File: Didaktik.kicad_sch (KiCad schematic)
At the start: 102 parts, among them J2 Conn_01x04_MountingPin, SW1 SW_Push, SW10 SW_Push_45deg, SW11 SW_Push_45deg, SW12 SW_Push_45deg, SW13 SW_Push_45deg, SW14 SW_Push_45deg, SW15 SW_Push_45deg, SW16 SW_Push_45deg, SW17 SW_Push_45deg, SW18 SW_Push_45deg, SW19 SW_Push_45deg, SW2 SW_Push_45deg, SW20 SW_Push_45deg, SW21 SW_Push_45deg, SW22 SW_Push_45deg, SW23 SW_Push_45deg, SW24 SW_Push_45deg, SW25 SW_Push_45deg, SW26 SW_Push_45deg, SW27 SW_Push_45deg, SW28 SW_Push_45deg, SW29 SW_Push_45deg, SW3 SW_Push_45deg, SW30 SW_Push_45deg, SW31 SW_Push_45deg, SW32 SW_Push_45deg, SW33 SW_Push_45deg, SW34 SW_Push_45deg, SW35 SW_Push_45deg, SW36 SW_Push_45deg, SW37 SW_Push_45deg, SW38 SW_Push_45deg, SW39 SW_Push_45deg, SW4 SW_Push_45deg, SW40 SW_Push_45deg, SW41 SW_Push_45deg, SW5 SW_Push_45deg, SW6 SW_Push_45deg, SW7 SW_Push_45deg, SW8 SW_Push_45deg, SW9 SW_Push_45deg, U1 ATmega32U4-M, Y1 Crystal_GND24_Small

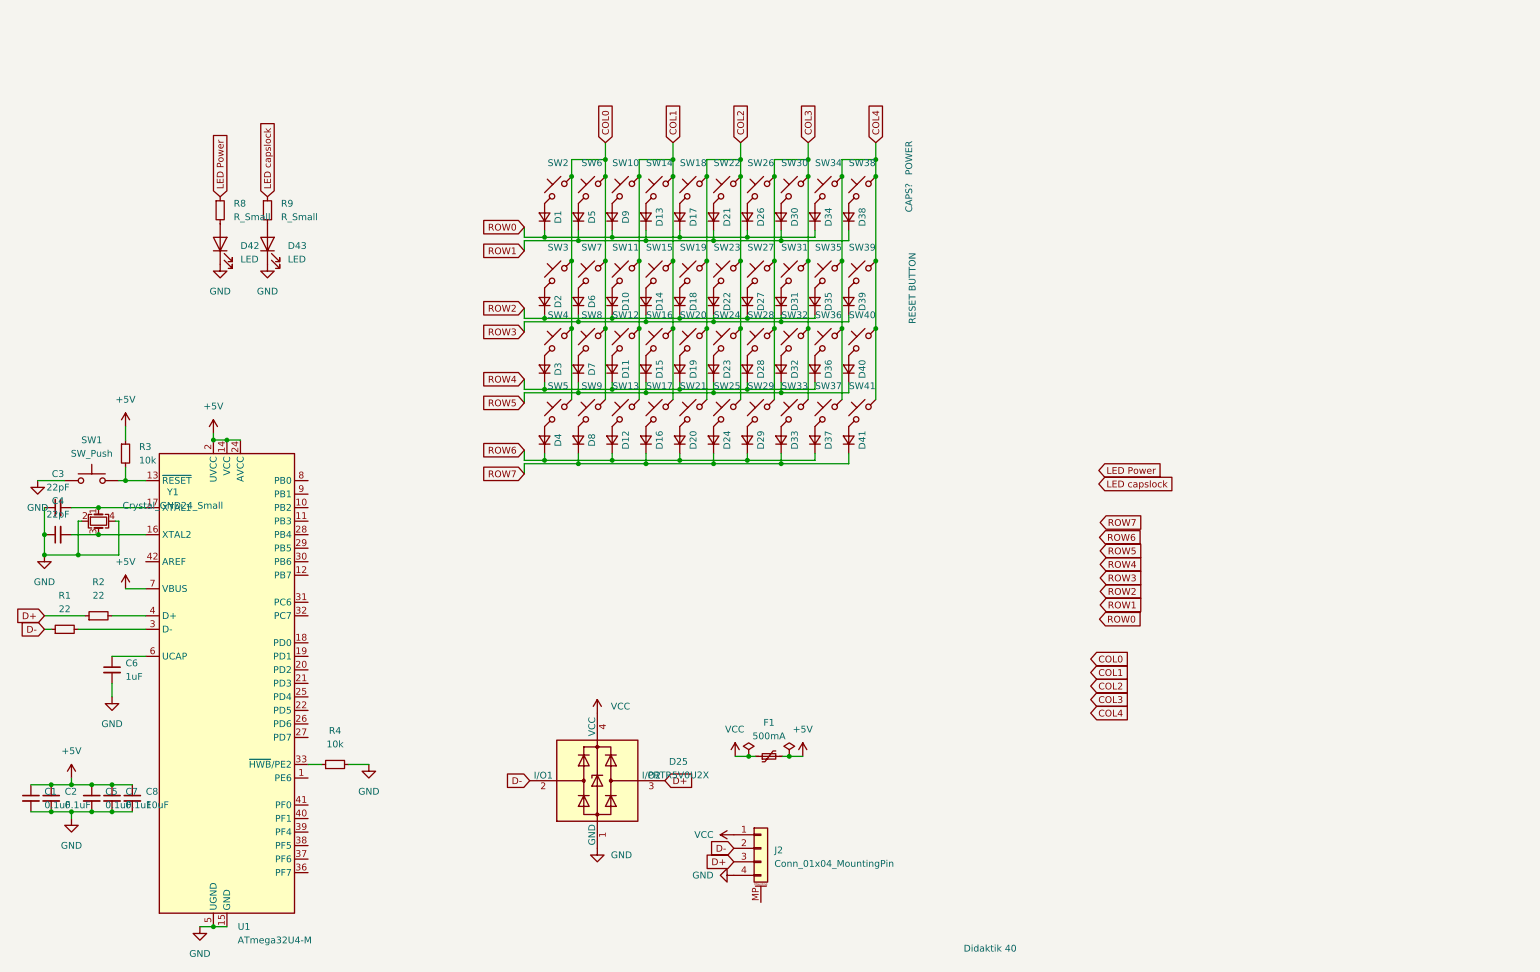
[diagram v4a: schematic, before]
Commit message: all traces routed, schematics cleaned up
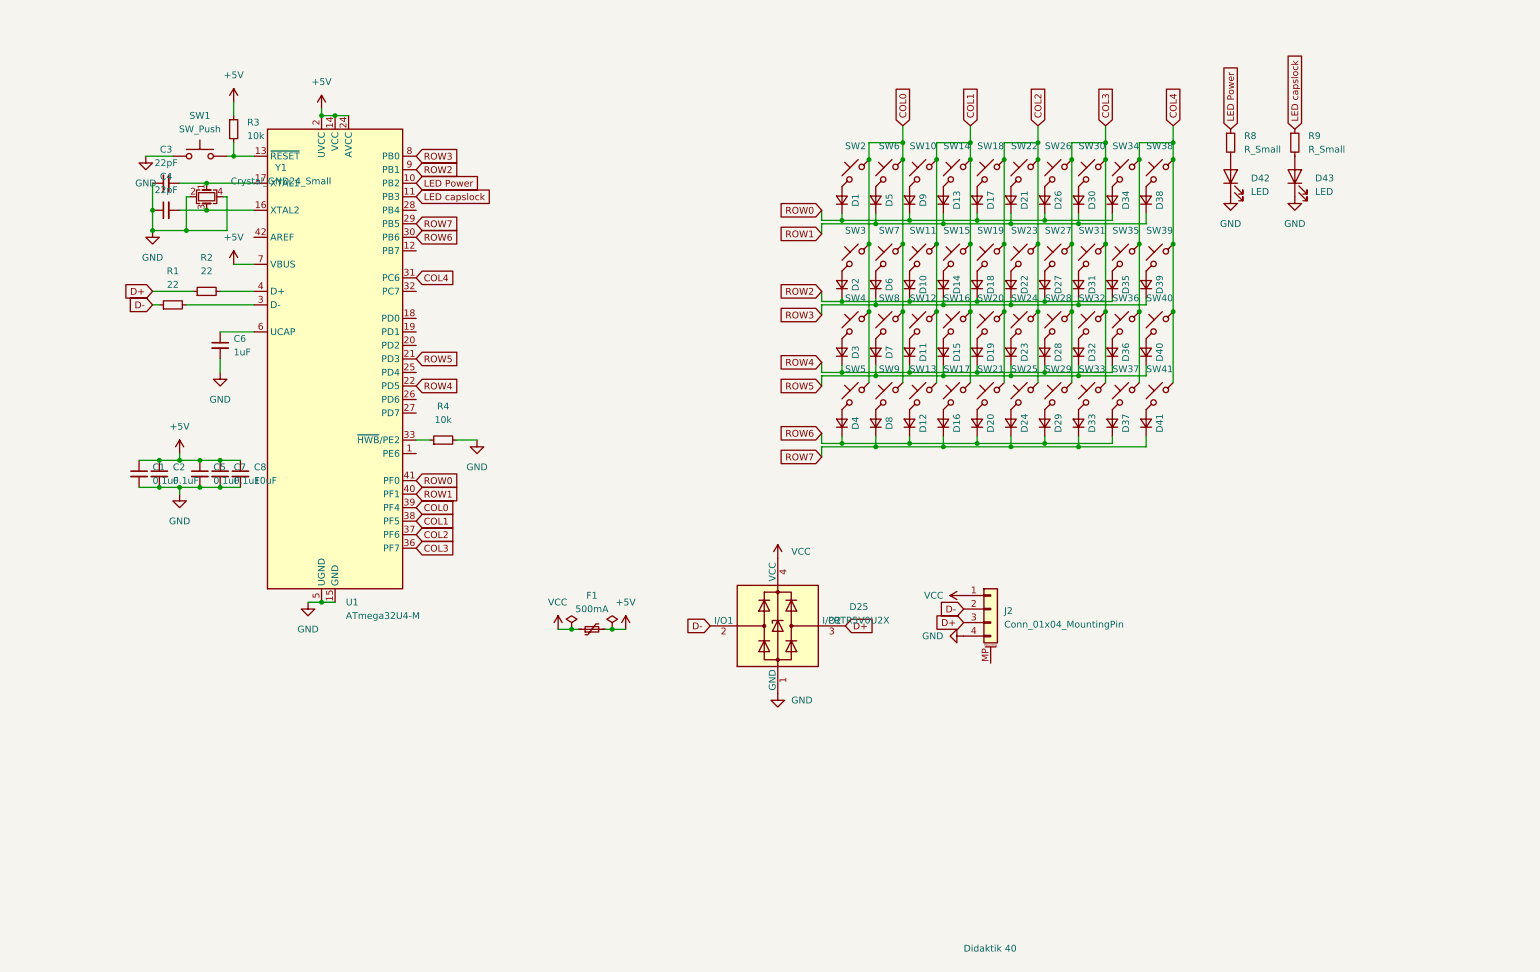
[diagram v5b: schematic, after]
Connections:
- net COL0: now also U1.39 (PF4)
- net COL1: now also U1.38 (PF5)
- net COL2: now also U1.37 (PF6)
- net COL3: now also U1.36 (PF7)
- net COL4: now also U1.31 (PC6)
- net LED Power: now also U1.10 (PB2)
- net LED capslock: now also U1.11 (PB3)
- net ROW0: now also U1.41 (PF0)
- net ROW1: now also U1.40 (PF1)
- net ROW2: now also U1.9 (PB1)
- net ROW3: now also U1.8 (PB0)
- net ROW4: now also U1.22 (PD5)
- net ROW5: now also U1.21 (PD3)
- net ROW6: now also U1.30 (PB6)
- net ROW7: now also U1.29 (PB5)
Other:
- note removed: "CAPS?"
- note removed: "POWER"
- note removed: "RESET BUTTON"
- moved on the sheet: C1, C2, C3, C4, C5, C6, C7, C8, D1, D10, D11, D12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

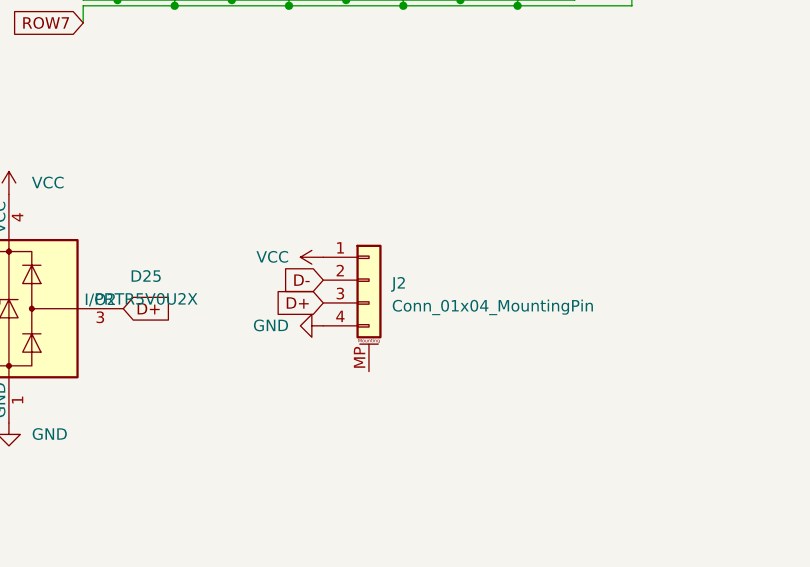
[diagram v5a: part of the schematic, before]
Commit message: full routing, silkscreens, zones
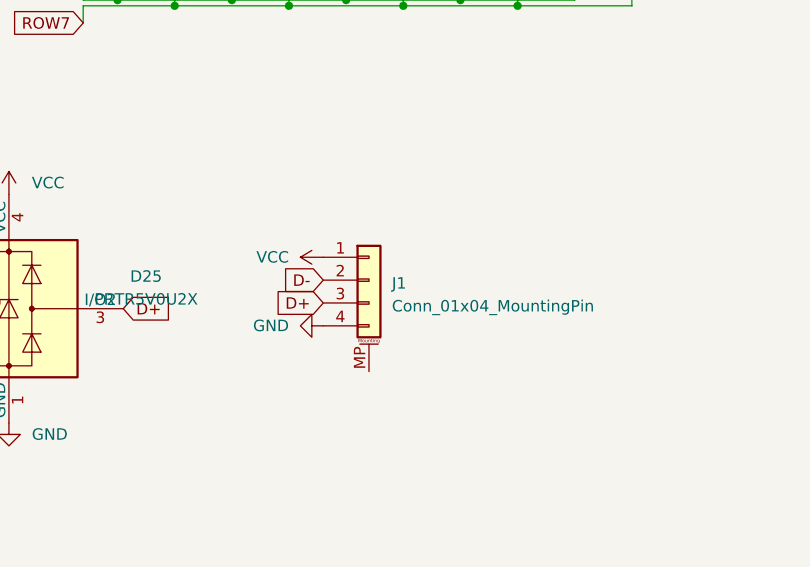
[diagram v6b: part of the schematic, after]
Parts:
- renumbered J2 to J1
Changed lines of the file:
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@@
   (symbol (lib_id "Connector_Generic_MountingPin:Conn_01x04_MountingPin") (at 193.04 125.73 0) (unit 1)
     (in_bom yes) (on_board yes) (fields_autoplaced)
-    (property "Reference" "J2" (id 0) (at 195.58 126.0855 0)
+    (property "Reference" "J1" (id 0) (at 195.58 126.0855 0)
       (effects (font (size 1.27 1.27)) (justify left))
     )
@@
     )
     (path "/773ca0f3-ad89-40fc-bb52-d706b4c154be"
-      (reference "J2") (unit 1) (value "Conn_01x04_MountingPin") (footprint "random-keyboard-parts:JST-SR-4")
+      (reference "J1") (unit 1) (value "Conn_01x04_MountingPin") (footprint "random-keyboard-parts:JST-SR-4")
     )
     (path "/1b233532-9656-4e4e-a0b7-8260db2f2d5f"

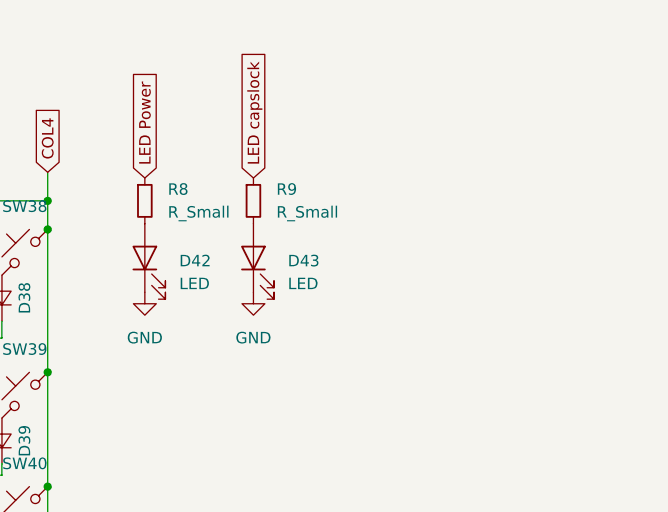
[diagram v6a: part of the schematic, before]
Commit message: created switchplate 40, cleaned 40s pcb. finished schematics for 45. created pcb project for 45
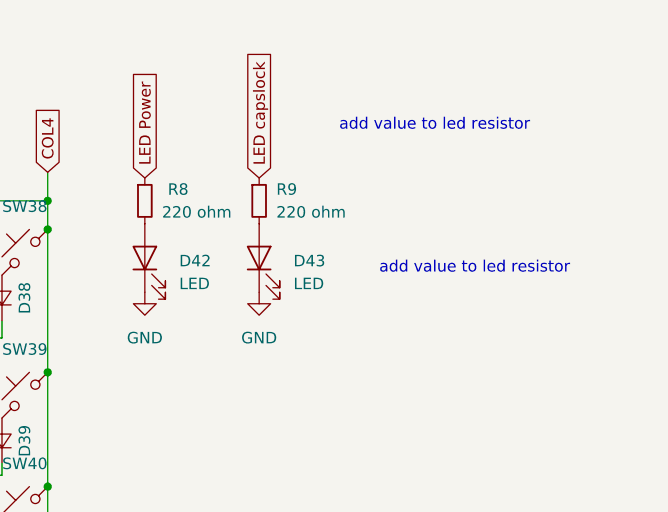
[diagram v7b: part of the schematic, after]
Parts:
- R8, R9: value R_Small -> 220 ohm
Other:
- note added: "add value to led resistor"
- moved on the sheet: D43, R9
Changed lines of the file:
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@@
+    (effects (font (size 1.27 1.27)) (justify left bottom))
+  )
+  (text "add value to led resistor" (at 259.715 30.48 0)
+    (effects (font (size 1.27 1.27)) (justify left bottom))
+  )
+  (text "add value to led resistor" (at 264.16 46.355 0)
     (effects (font (size 1.27 1.27)) (justify left bottom))
   )
@@
     )
   )
-  (global_label "LED capslock" (shape input) (at 250.19 35.56 90) (fields_autoplaced)
+  (global_label "LED capslock" (shape input) (at 250.825 35.56 90) (fields_autoplaced)
     (effects (font (size 1.27 1.27)) (justify left))
-    (property "Intersheet References" "${INTERSHEET_REFS}" (id 0) (at 250.1106 20.3864 90)
+    (property "Intersheet References" "${INTERSHEET_REFS}" (id 0) (at 250.7456 20.3864 90)
       (effects (font (size 1.27 1.27)) (justify left) hide)
     )
@@
     (pin "1")
   )
-  (symbol (lib_id "ComboDiode:R_Small") (at 250.19 38.1 0) (unit 1)
+  (symbol (lib_id "ComboDiode:R_Small") (at 250.825 38.1 0) (unit 1)
     (in_bom yes) (on_board yes) (fields_autoplaced)
     (property "Reference" "R9" (id 0) (at 252.73 36.8299 0)
       (effects (font (size 1.27 1.27)) (justify left))
     )
-    (property "Value" "R_Small" (id 1) (at 252.73 39.3699 0)
-      (effects (font (size 1.27 1.27)) (justify left))
-    )
-    (property "Footprint" "Resistor_SMD:R_0402_1005Metric" (id 2) (at 250.19 38.1 0)
-      (effects (font (size 1.27 1.27)) hide)
-    )
-    (property "Datasheet" "" (id 3) (at 250.19 38.1 0)
+    (property "Value" "220 ohm" (id 1) (at 252.73 39.3699 0)
+      (effects (font (size 1.27 1.27)) (justify left))
+    )
+    (property "Footprint" "Resistor_SMD:R_0402_1005Metric" (id 2) (at 250.825 38.1 0)
+      (effects (font (size 1.27 1.27)) hide)
+    )
+    (property "Datasheet" "" (id 3) (at 250.825 38.1 0)
       (effects (font (size 1.27 1.27)) hide)
     )
@@
     (pin "2")
   )
-  (symbol (lib_id "power:GND") (at 250.19 48.26 0) (unit 1)
-    (in_bom yes) (on_board yes) (fields_autoplaced)
-    (property "Reference" "#PWR0123" (id 0) (at 250.19 54.61 0)
-      (effects (font (size 1.27 1.27)) hide)
-    )
-    (property "Value" "GND" (id 1) (at 250.19 53.34 0))
-    (property "Footprint" "" (id 2) (at 250.19 48.26 0)
-      (effects (font (size 1.27 1.27)) hide)
-    )
-    (property "Datasheet" "" (id 3) (at 250.19 48.26 0)
+  (symbol (lib_id "power:GND") (at 250.825 48.26 0) (unit 1)
+    (in_bom yes) (on_board yes) (fields_autoplaced)
+    (property "Reference" "#PWR0123" (id 0) (at 250.825 54.61 0)
+      (effects (font (size 1.27 1.27)) hide)
+    )
+    (property "Value" "GND" (id 1) (at 250.825 53.34 0))
+    (property "Footprint" "" (id 2) (at 250.825 48.26 0)
+      (effects (font (size 1.27 1.27)) hide)
+    )
+    (property "Datasheet" "" (id 3) (at 250.825 48.26 0)
       (effects (font (size 1.27 1.27)) hide)
     )
@@
   )
   (symbol (lib_id "ComboDiode:R_Small") (at 238.125 38.1 0) (unit 1)
-    (in_bom yes) (on_board yes) (fields_autoplaced)
+    (in_bom yes) (on_board yes)
     (property "Reference" "R8" (id 0) (at 240.665 36.8299 0)
       (effects (font (size 1.27 1.27)) (justify left))
     )
-    (property "Value" "R_Small" (id 1) (at 240.665 39.3699 0)
+    (property "Value" "220 ohm" (id 1) (at 240.03 39.37 0)
       (effects (font (size 1.27 1.27)) (justify left))
     )
@@
     (pin "1")
   )
-  (symbol (lib_id "ComboDiode:LED") (at 250.19 44.45 90) (unit 1)
-    (in_bom yes) (on_board yes) (fields_autoplaced)
-    (property "Reference" "D43" (id 0) (at 254 44.7801 90)
+  (symbol (lib_id "ComboDiode:LED") (at 250.825 44.45 90) (unit 1)
+    (in_bom yes) (on_board yes) (fields_autoplaced)
+    (property "Reference" "D43" (id 0) (at 254.635 44.7801 90)
       (effects (font (size 1.27 1.27)) (justify right))
     )
-    (property "Value" "LED" (id 1) (at 254 47.3201 90)
+    (property "Value" "LED" (id 1) (at 254.635 47.3201 90)
       (effects (font (size 1.27 1.27)) (justify right))
     )
-    (property "Footprint" "Keebio-Parts:LED_3mm" (id 2) (at 250.19 44.45 0)
-      (effects (font (size 1.27 1.27)) hide)
-    )
-    (property "Datasheet" "" (id 3) (at 250.19 44.45 0)
+    (property "Footprint" "Keebio-Parts:LED_3mm" (id 2) (at 250.825 44.45 0)
+      (effects (font (size 1.27 1.27)) hide)
+    )
+    (property "Datasheet" "" (id 3) (at 250.825 44.45 0)
       (effects (font (size 1.27 1.27)) hide)
     )
@@
     )
     (path "/aa3e1884-38d9-45ba-ac50-ac00233610fb"
-      (reference "R8") (unit 1) (value "R_Small") (footprint "Resistor_SMD:R_0402_1005Metric")
+      (reference "R8") (unit 1) (value "220 ohm") (footprint "Resistor_SMD:R_0402_1005Metric")
     )
     (path "/12715afe-3bd4-4008-a3e0-15f3bd502da1"
-      (reference "R9") (unit 1) (value "R_Small") (footprint "Resistor_SMD:R_0402_1005Metric")
+      (reference "R9") (unit 1) (value "220 ohm") (footprint "Resistor_SMD:R_0402_1005Metric")
     )
     (path "/24a36d74-2c9b-468a-8a3d-4eb2fe2b6c67"
